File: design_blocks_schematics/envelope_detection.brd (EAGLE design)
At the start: 15.2 x 18.5 mm, 13 parts

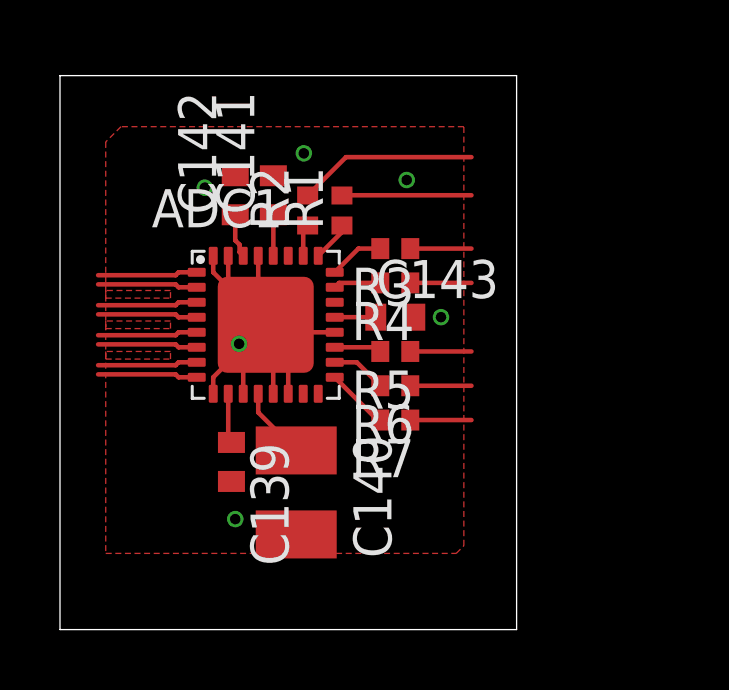
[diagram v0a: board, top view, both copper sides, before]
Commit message: updated board size of dbl added envelope detection: - simulation - design block
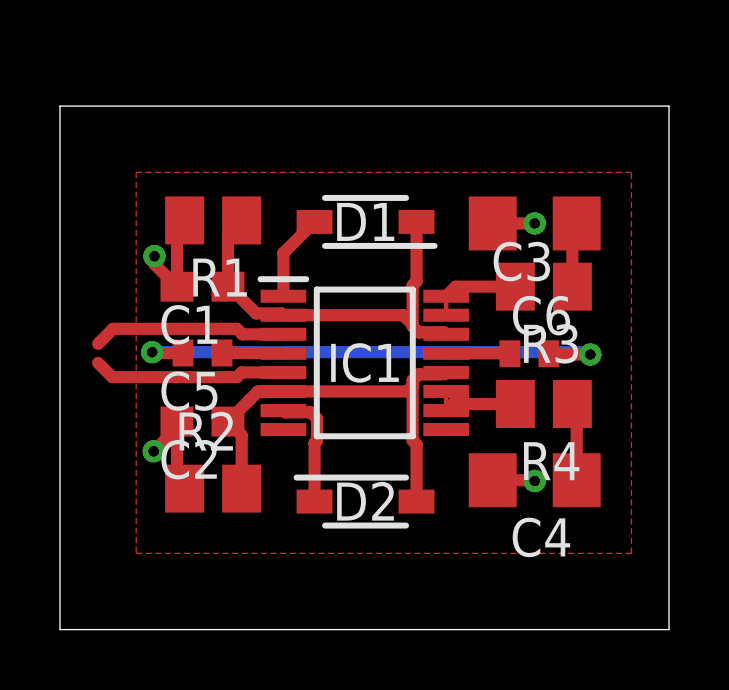
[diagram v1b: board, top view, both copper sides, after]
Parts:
- removed ADC1: LTC2344-16, wouter:QFN32
- removed C139, C142, C143: 0.1uf, rcl:C0402
- removed C140: 47uf 10V, rcl:C1210
- removed C141: 2.2uf, rcl:C0402
- removed R5, R6, R7: 33R, rcl:R0402
- added C1, C2: 100n, rcl:C0603
- added C3, C4: 100n C0G, rcl:C1206
- added C5, C6: 3.3u, rcl:C0402
- added D1, D2: MBR0520L, wouter:SOD3816X128N
- added IC1: LT6238HGN#PBF, wouter:SOP64P601X175-16N
- R1, R2: value 33R -> 300R; device rcl:R0402 -> rcl:M0805
- R3, R4: value 33R -> 82R; device rcl:R0402 -> rcl:M0805
- moved R2 9.79 mm to (5.11, 4.70), turned to 0 degrees
- moved R4 6.39 mm to (16.1, 7.52)
- moved R3 5.11 mm to (16.1, 11.4)
- moved R1 4.31 mm to (5.11, 13.6), turned to 180 degrees
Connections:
- removed net /CS: ADC1.27
- removed net ADIN0_N: ADC1.7
- removed net ADIN0_P: ADC1.8
- removed net ADIN1_N: ADC1.5
- removed net ADIN1_P: ADC1.6
- removed net ADIN2_N: ADC1.3
- removed net ADIN2_P: ADC1.4
- removed net ADIN3_N: ADC1.1
- removed net ADIN3_P: ADC1.2
- removed net BUSY: R2.2
- removed net CNV: ADC1.15
- removed net N$1: ADC1.24, R3.2
- removed net N$2: ADC1.23, R4.2
- removed net N$3: ADC1.19, R5.2
- removed net N$4: ADC1.18, R6.2
- removed net N$5: ADC1.17, R7.2
- removed net N$81: ADC1.10, C139.1
- removed net N$82: ADC1.12, C140.1
- removed net N$83: ADC1.28, C141.1
- removed net N1: ADC1.26, R2.1
- removed net N2: ADC1.25, R1.1
- removed net OVDD: ADC1.21, C143.1
- removed net SCKI: R5.1
- removed net SDI: R1.2
- removed net SDO0: R7.1
- removed net SDO1: R6.1
- removed net SDO2: R4.1
- removed net SDO3: R3.1
- new net +IN_C: C1.1, D1.1, IC1.14, IC1.2, R1.1
- new net +IN_D: C2.1, D2.2, IC1.12, IC1.6, R2.2
- new net -5V: C6.1, IC1.13
- new net IN_1: IC1.3
- new net IN_2: IC1.5
- new net OUT_1: C3.1, R3.1
- new net OUT_2: C4.1, R4.1
- new net OUT_A: D1.2, IC1.1
- new net OUT_B: IC1.10, IC1.11, R4.2
- new net OUT_C: D2.1, IC1.7
- new net OUT_D: IC1.15, IC1.16, R3.2
- new net VCOM: C1.2, C2.2, C3.2, C4.2, R1.2, R2.1
- net +5V: now also C5.1, IC1.4; no longer ADC1.30, C142.1
- net GND: now also C5.2, C6.2; no longer ADC1.11, ADC1.13, ADC1.14, ADC1.20, ADC1.29, ADC1.31, ADC1.32, ADC1.9, ADC1.EXP, C139.2, C140.2, C141.2, C142.2, C143.2
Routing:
- net +IN_C: track 0.00 -> 16.9 mm
- net +IN_D: track 0.00 -> 16.0 mm
- net VCOM: track 0.00 -> 10.1 mm, vias 0 -> 4
- net IN_1: track 0.00 -> 6.46 mm
- net IN_2: track 0.00 -> 6.44 mm
- net BUSY: track 5.99 -> 0.00 mm
- net GND: track 21.6 -> 17.1 mm, vias 6 -> 2
- net SDI: track 4.32 -> 0.00 mm
- net OUT_C: track 0.00 -> 4.03 mm
- net ADIN3_P: track 3.33 -> 0.00 mm
- net ADIN3_N: track 3.33 -> 0.00 mm
- net ADIN2_P: track 3.33 -> 0.00 mm
- net ADIN2_N: track 3.33 -> 0.00 mm
- net ADIN1_P: track 3.33 -> 0.00 mm
- net ADIN1_N: track 3.33 -> 0.00 mm
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- added copper zone on layer 1, net VCOM
- removed copper zone on layer 1, net GND
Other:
- board size 15.2 x 18.5 mm -> 20.3 x 17.4 mm
